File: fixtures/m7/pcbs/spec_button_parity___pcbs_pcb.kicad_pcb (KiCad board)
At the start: 2 copper layers, 1 part

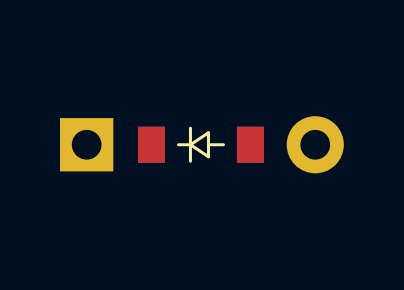
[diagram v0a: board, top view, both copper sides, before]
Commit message: Expand footprint specs and add JS footprints plan
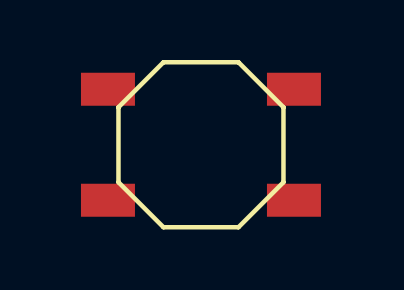
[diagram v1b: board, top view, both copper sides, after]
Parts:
- removed D1: , ComboDiode
- added B1: , E73:SW_TACT_ALPS_SKQGABE010, F.Cu at (0.00, 0.00)
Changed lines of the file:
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@@
   )
   (net 0 "")
-(net 1 "D_FROM")
-(net 2 "D_TO")
+(net 1 "BTN_FROM")
+(net 2 "BTN_TO")
   (net_class Default "This is the default net class."
     (clearance 0.2)
@@
     (uvia_drill 0.1)
     (add_net "")
-(add_net "D_FROM")
-(add_net "D_TO")
+(add_net "BTN_FROM")
+(add_net "BTN_TO")
   )
-        (module ComboDiode (layer F.Cu)
+        (module E73:SW_TACT_ALPS_SKQGABE010 (layer F.Cu)
+            (descr "Low-profile SMD Tactile Switch, https://www.e-switch.com/product-catalog/tact/product-lines/tl3342-series-low-profile-smt-tact-switch")
+            (tags "SPST Tactile Switch")
             (at 0 0 0)
-            (fp_text reference "D1" (at 0 0) (layer F.SilkS) hide (effects (font (size 1.27 1.27) (thickness 0.15))))
+            (fp_text reference "B1" (at 0 0) (layer F.SilkS) hide (effects (font (size 1.27 1.27) (thickness 0.15))))
             (fp_text value "" (at 0 0) (layer F.SilkS) hide (effects (font (size 1.27 1.27) (thickness 0.15))))
-            (fp_line (start 0.25 0) (end 0.75 0) (layer F.SilkS) (width 0.1))
-            (fp_line (start 0.25 0.4) (end -0.35 0) (layer F.SilkS) (width 0.1))
-            (fp_line (start 0.25 -0.4) (end 0.25 0.4) (layer F.SilkS) (width 0.1))
-            (fp_line (start -0.35 0) (end 0.25 -0.4) (layer F.SilkS) (width 0.1))
-            (fp_line (start -0.35 0) (end -0.35 0.55) (layer F.SilkS) (width 0.1))
-            (fp_line (start -0.35 0) (end -0.35 -0.55) (layer F.SilkS) (width 0.1))
-            (fp_line (start -0.75 0) (end -0.35 0) (layer F.SilkS) (width 0.1))
-            (fp_line (start 0.25 0) (end 0.75 0) (layer B.SilkS) (width 0.1))
-            (fp_line (start 0.25 0.4) (end -0.35 0) (layer B.SilkS) (width 0.1))
-            (fp_line (start 0.25 -0.4) (end 0.25 0.4) (layer B.SilkS) (width 0.1))
-            (fp_line (start -0.35 0) (end 0.25 -0.4) (layer B.SilkS) (width 0.1))
-            (fp_line (start -0.35 0) (end -0.35 0.55) (layer B.SilkS) (width 0.1))
-            (fp_line (start -0.35 0) (end -0.35 -0.55) (layer B.SilkS) (width 0.1))
-            (fp_line (start -0.75 0) (end -0.35 0) (layer B.SilkS) (width 0.1))
-            (pad 1 smd rect (at -1.65 0 0) (size 0.9 1.2) (layers F.Cu F.Paste F.Mask) (net 2 "D_TO"))
-            (pad 2 smd rect (at 1.65 0 0) (size 0.9 1.2) (layers B.Cu B.Paste B.Mask) (net 1 "D_FROM"))
-            (pad 1 smd rect (at -1.65 0 0) (size 0.9 1.2) (layers B.Cu B.Paste B.Mask) (net 2 "D_TO"))
-            (pad 2 smd rect (at 1.65 0 0) (size 0.9 1.2) (layers F.Cu F.Paste F.Mask) (net 1 "D_FROM"))
-            (pad 1 thru_hole rect (at -3.81 0 0) (size 1.778 1.778) (drill 0.9906) (layers *.Cu *.Mask) (net 2 "D_TO"))
-            (pad 2 thru_hole circle (at 3.81 0 0) (size 1.905 1.905) (drill 0.9906) (layers *.Cu *.Mask) (net 1 "D_FROM"))
+            (fp_line (start 2.75 1.25) (end 1.25 2.75) (layer F.SilkS) (width 0.15))
+            (fp_line (start 2.75 -1.25) (end 1.25 -2.75) (layer F.SilkS) (width 0.15))
+            (fp_line (start 2.75 -1.25) (end 2.75 1.25) (layer F.SilkS) (width 0.15))
+            (fp_line (start -1.25 2.75) (end 1.25 2.75) (layer F.SilkS) (width 0.15))
+            (fp_line (start -1.25 -2.75) (end 1.25 -2.75) (layer F.SilkS) (width 0.15))
+            (fp_line (start -2.75 1.25) (end -1.25 2.75) (layer F.SilkS) (width 0.15))
+            (fp_line (start -2.75 -1.25) (end -1.25 -2.75) (layer F.SilkS) (width 0.15))
+            (fp_line (start -2.75 -1.25) (end -2.75 1.25) (layer F.SilkS) (width 0.15))
+            (pad 1 smd rect (at -3.1 -1.85 0) (size 1.8 1.1) (layers F.Cu F.Paste F.Mask) (net 1 "BTN_FROM"))
+            (pad 1 smd rect (at 3.1 -1.85 0) (size 1.8 1.1) (layers F.Cu F.Paste F.Mask) (net 1 "BTN_FROM"))
+            (pad 2 smd rect (at -3.1 1.85 0) (size 1.8 1.1) (layers F.Cu F.Paste F.Mask) (net 2 "BTN_TO"))
+            (pad 2 smd rect (at 3.1 1.85 0) (size 1.8 1.1) (layers F.Cu F.Paste F.Mask) (net 2 "BTN_TO"))
         )
 )
